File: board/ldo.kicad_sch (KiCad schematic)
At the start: 6 parts, among them J3 Conn_01x03_Male, U1 TLV743P

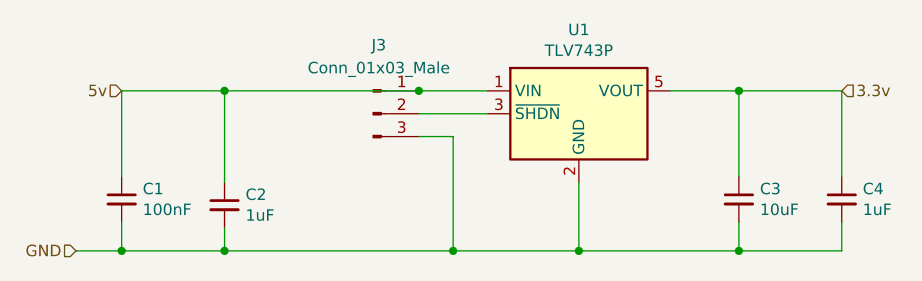
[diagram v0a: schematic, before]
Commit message: modernized layout to use 000 generic power symbols. the layout and thereofore the hardware version number is unaffected
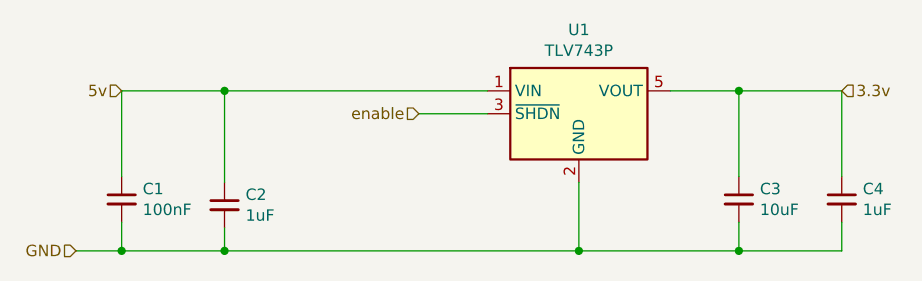
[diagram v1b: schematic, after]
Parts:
- removed J3: Conn_01x03_Male, Connector_PinHeader_2.54mm:PinHeader_1x03_P2.54mm_Vertical, symbol Connector:Conn_01x03_Male
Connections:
- net enable: now reaches U1.3 (~{SHDN})
